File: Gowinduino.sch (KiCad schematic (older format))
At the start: 61 parts, among them J1 Power, J2 Analog, J3 Digital, J4 Digital, J5 SPI, J6 JTAG, J8 12V, Q1 2N7002, Q2 2N7002, SW1 Mode, SW2 Reset, U1 GW1NSR-4CQN48P, U10 SN74AVC4T245PW, U11 MAX811SEUS-T, U12 SN74LVC1T45DBV, U2 W25Q32JVSS, U3 TXB0104PW, U4 MP2122, U8 L7805, U9 FP6161, X1 XO32

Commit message: FInals: front-side silkscreens
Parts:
- added R19: 1k, Resistor_SMD:R_0603_1608Metric_Pad0.98x0.95mm_HandSolder, symbol Device:R_Small
- R17: value 10k -> 4.7k
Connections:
- net GND: now also R19.2
- net SCLK: now also R19.1
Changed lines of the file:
@@
 L power:GND #PWR0115
 U 1 1 60832B7B
-P 6700 2800
-F 0 "#PWR0115" H 6700 2550 50  0001 C CNN
-F 1 "GND" H 6705 2627 50  0000 C CNN
-F 2 "" H 6700 2800 50  0001 C CNN
-F 3 "" H 6700 2800 50  0001 C CNN
-	1    6700 2800
+P 6700 2900
+F 0 "#PWR0115" H 6700 2650 50  0001 C CNN
+F 1 "GND" H 6705 2727 50  0000 C CNN
+F 2 "" H 6700 2900 50  0001 C CNN
+F 3 "" H 6700 2900 50  0001 C CNN
+	1    6700 2900
 	1    0    0    -1
 $EndComp
@@
 P 8700 2000
 F 0 "R17" H 8759 2046 50  0000 L CNN
-F 1 "10k" H 8759 1955 50  0000 L CNN
+F 1 "4.7k" H 8759 1955 50  0000 L CNN
 F 2 "Resistor_SMD:R_0603_1608Metric_Pad0.98x0.95mm_HandSolder" H 8700 2000 50  0001 C CNN
 F 3 "~" H 8700 2000 50  0001 C CNN
@@
 	7300 5200 7900 5200
 NoConn ~ 7200 5100
+$Comp
+L Device:R_Small R19
+U 1 1 61AC0DB1
+P 6000 2600
+F 0 "R19" H 6059 2646 50  0000 L CNN
+F 1 "1k" H 6059 2555 50  0000 L CNN
+F 2 "Resistor_SMD:R_0603_1608Metric_Pad0.98x0.95mm_HandSolder" H 6000 2600 50  0001 C CNN
+F 3 "~" H 6000 2600 50  0001 C CNN
+	1    6000 2600
+	1    0    0    -1
+$EndComp
+Wire Wire Line
+	6000 2500 6000 2400
+Wire Wire Line
+	6700 2800 6000 2800
+Wire Wire Line
+	6000 2800 6000 2700
+Connection ~ 6700 2800
+Wire Wire Line
+	6700 2800 6700 2900
 $EndSCHEMATC

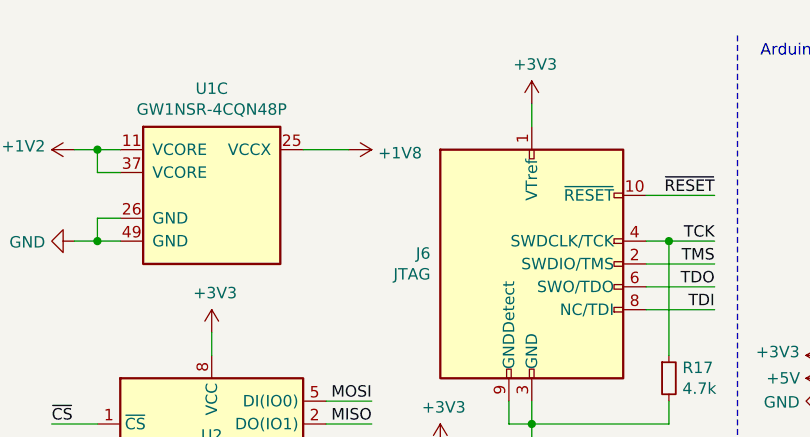
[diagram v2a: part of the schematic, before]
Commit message: OSHW and ESD symbols
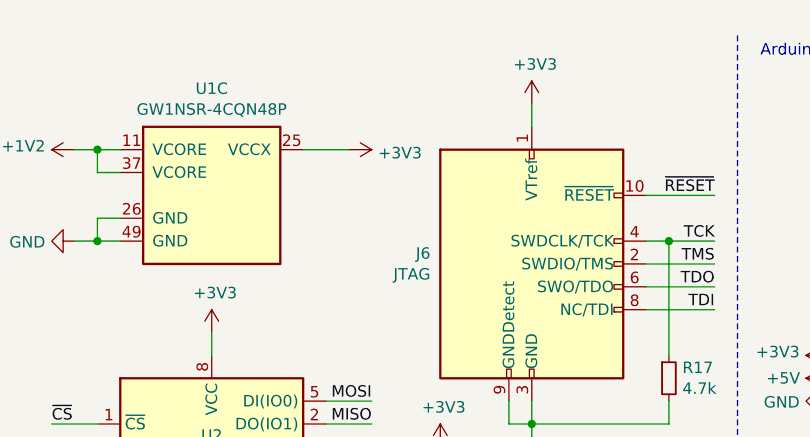
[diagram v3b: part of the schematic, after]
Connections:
- net +1V8: no longer U1.25 (VCCX)
- net +3V3: now also U1.25 (VCCX)
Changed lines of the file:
@@
 	1    0    0    -1
-$EndComp
-$Comp
-L power:+1V8 #PWR0111
-U 1 1 6081734C
-P 7300 1000
-F 0 "#PWR0111" H 7300 850 50  0001 C CNN
-F 1 "+1V8" V 7315 1128 50  0000 L CNN
-F 2 "" H 7300 1000 50  0001 C CNN
-F 3 "" H 7300 1000 50  0001 C CNN
-	1    7300 1000
-	0    1    1    0
 $EndComp
 Wire Wire Line
@@
 Wire Wire Line
 	6700 2800 6700 2900
+$Comp
+L power:+3V3 #PWR?
+U 1 1 61B37E61
+P 7300 1000
+F 0 "#PWR?" H 7300 850 50  0001 C CNN
+F 1 "+3V3" V 7315 1128 50  0000 L CNN
+F 2 "" H 7300 1000 50  0001 C CNN
+F 3 "" H 7300 1000 50  0001 C CNN
+	1    7300 1000
+	0    1    1    0
+$EndComp
 $EndSCHEMATC
